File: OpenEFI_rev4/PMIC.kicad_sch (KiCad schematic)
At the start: 40 parts, among them U1 MCZ33810EK, U21 TC4424A, U24 TC4424A, U29 TC4424A, U30 TC4424A

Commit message: update sensors/connector pinout, added rtc vbatt backup
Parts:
- removed R129, R83: 10k, Resistor_SMD:R_0805_2012Metric, symbol Device:R
- added R58 (x2): 10k, Resistor_SMD:R_0805_2012Metric, symbol Device:R_Small
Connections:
- net GND: now also R58.1, R58.1
- net PMIC1_ENABLE: now also R58.2, R58.2
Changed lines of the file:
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@@
     (stroke (width 0) (type default))
   )
-  (wire (pts (xy 51.435 141.605) (xy 51.435 142.875))
+  (wire (pts (xy 48.26 143.51) (xy 48.26 144.78))
     (stroke (width 0) (type default))
   )
@@
     (stroke (width 0) (type solid))
   )
-  (wire (pts (xy 49.53 52.07) (xy 49.53 53.34))
+  (wire (pts (xy 49.53 54.61) (xy 49.53 55.88))
     (stroke (width 0) (type default))
   )
@@
     (effects (font (size 0.8 0.8)) (justify right bottom))
   )
-  (label "PMIC1_ENABLE" (at 51.435 141.605 180) (fields_autoplaced)
+  (label "PMIC1_ENABLE" (at 48.26 143.51 180) (fields_autoplaced)
     (effects (font (size 0.7874 0.7874)) (justify right bottom))
   )
-  (label "PMIC1_ENABLE" (at 49.53 52.07 180) (fields_autoplaced)
+  (label "PMIC1_ENABLE" (at 49.53 54.61 180) (fields_autoplaced)
     (effects (font (size 0.7874 0.7874)) (justify right bottom))
   )
@@
     )
   )
-  (symbol (lib_name "GND_1") (lib_id "power:GND") (at 51.435 150.495 0) (unit 1)
+  (symbol (lib_name "GND_1") (lib_id "power:GND") (at 48.26 149.86 0) (unit 1)
     (in_bom yes) (on_board yes) (dnp no) (fields_autoplaced)
-    (property "Reference" "#PWR02" (at 51.435 156.845 0)
+    (property "Reference" "#PWR02" (at 48.26 156.21 0)
       (effects (font (size 1.27 1.27)) hide)
     )
-    (property "Value" "GND" (at 51.435 154.94 0)
+    (property "Value" "GND" (at 48.26 154.305 0)
       (effects (font (size 1.27 1.27)))
     )
-    (property "Footprint" "" (at 51.435 150.495 0)
+    (property "Footprint" "" (at 48.26 149.86 0)
       (effects (font (size 1.27 1.27)) hide)
     )
-    (property "Datasheet" "" (at 51.435 150.495 0)
+    (property "Datasheet" "" (at 48.26 149.86 0)
       (effects (font (size 1.27 1.27)) hide)
     )
@@
     )
   )
+  (symbol (lib_id "Device:R_Small") (at 49.53 58.42 0) (mirror x) (unit 1)
+    (in_bom yes) (on_board yes) (dnp no)
+    (property "Reference" "R58" (at 51.435 58.42 90)
+      (effects (font (size 1.27 1.27)))
+    )
+    (property "Value" "10k" (at 47.625 58.42 90)
+      (effects (font (size 1.27 1.27)))
+    )
+    (property "Footprint" "Resistor_SMD:R_0805_2012Metric" (at 49.53 58.42 0)
+      (effects (font (size 1.27 1.27)) hide)
+    )
+    (property "Datasheet" "~" (at 49.53 58.42 0)
+      (effects (font (size 1.27 1.27)) hide)
+    )
+    (property "LCSC" "C17414" (at 49.53 58.42 90)
+      (effects (font (size 0.889 0.889)) hide)
+    )
+    (pin "1")
+    (pin "2")
+    (instances
+      (project "OpenEFI_rev4"
+        (path "/b282ce4b-c3d0-4c94-b06c-73b92bb672a9"
+          (reference "R58") (unit 1)
+        )
+        (path "/b282ce4b-c3d0-4c94-b06c-73b92bb672a9/00000000-0000-0000-0000-00005fa9324b"
+          (reference "R84") (unit 1)
+        )
+      )
+    )
+  )
   (symbol (lib_id "OpenEFI-STM32-rev3:MCZ33810EK") (at 78.105 51.435 0) (unit 1)
     (in_bom yes) (on_board yes) (dnp no)
@@
     )
   )
-  (symbol (lib_id "Device:R") (at 49.53 57.15 180) (unit 1)
-    (in_bom yes) (on_board yes) (dnp no)
-    (property "Reference" "R129" (at 47.752 58.3184 0)
-      (effects (font (size 1.27 1.27)) (justify left))
-    )
-    (property "Value" "10k" (at 47.752 56.007 0)
-      (effects (font (size 1.27 1.27)) (justify left))
-    )
-    (property "Footprint" "Resistor_SMD:R_0805_2012Metric" (at 51.308 57.15 90)
-      (effects (font (size 1.27 1.27)) hide)
-    )
-    (property "Datasheet" "~" (at 49.53 57.15 0)
-      (effects (font (size 1.27 1.27)) hide)
-    )
-    (property "Digikey Part Number" "311-10KARCT-ND" (at 49.53 57.15 0)
-      (effects (font (size 1.27 1.27)) hide)
-    )
-    (property "Manufacturer_Name" "Yageo" (at 49.53 57.15 0)
-      (effects (font (size 1.27 1.27)) hide)
-    )
-    (property "Manufacturer_Part_Number" "RC0805JR-0710KL" (at 49.53 57.15 0)
-      (effects (font (size 1.27 1.27)) hide)
-    )
-    (property "URL" "https://www.digikey.com/product-detail/en/yageo/RC0805JR-0710KL/311-10KARCT-ND/731188" (at 49.53 57.15 0)
-      (effects (font (size 1.27 1.27)) hide)
-    )
-    (pin "1")
-    (pin "2")
-    (instances
-      (project "OpenEFI_rev4"
-        (path "/b282ce4b-c3d0-4c94-b06c-73b92bb672a9/00000000-0000-0000-0000-00005fa9324b"
-          (reference "R129") (unit 1)
-        )
-      )
-      (project "DropBear"
-        (path "/ebe274a6-1c43-4fa2-9d2a-7756c5a7217c/00000000-0000-0000-0000-00005cb195fe"
-          (reference "R6") (unit 1)
-        )
-      )
-    )
-  )
   (symbol (lib_id "power:GND") (at 257.175 97.79 0) (unit 1)
     (in_bom yes) (on_board yes) (dnp no)
@@
     )
   )
-  (symbol (lib_id "Device:R") (at 51.435 146.685 180) (unit 1)
-    (in_bom yes) (on_board yes) (dnp no)
-    (property "Reference" "R83" (at 49.657 147.8534 0)
-      (effects (font (size 1.27 1.27)) (justify left))
-    )
-    (property "Value" "10k" (at 49.657 145.542 0)
-      (effects (font (size 1.27 1.27)) (justify left))
-    )
-    (property "Footprint" "Resistor_SMD:R_0805_2012Metric" (at 53.213 146.685 90)
-      (effects (font (size 1.27 1.27)) hide)
-    )
-    (property "Datasheet" "~" (at 51.435 146.685 0)
-      (effects (font (size 1.27 1.27)) hide)
-    )
-    (property "Digikey Part Number" "311-10KARCT-ND" (at 51.435 146.685 0)
-      (effects (font (size 1.27 1.27)) hide)
-    )
-    (property "Manufacturer_Name" "Yageo" (at 51.435 146.685 0)
-      (effects (font (size 1.27 1.27)) hide)
-    )
-    (property "Manufacturer_Part_Number" "RC0805JR-0710KL" (at 51.435 146.685 0)
-      (effects (font (size 1.27 1.27)) hide)
-    )
-    (property "URL" "https://www.digikey.com/product-detail/en/yageo/RC0805JR-0710KL/311-10KARCT-ND/731188" (at 51.435 146.685 0)
-      (effects (font (size 1.27 1.27)) hide)
-    )
-    (pin "1")
-    (pin "2")
-    (instances
-      (project "OpenEFI_rev4"
-        (path "/b282ce4b-c3d0-4c94-b06c-73b92bb672a9/00000000-0000-0000-0000-00005fa9324b"
-          (reference "R83") (unit 1)
-        )
-      )
-      (project "DropBear"
-        (path "/ebe274a6-1c43-4fa2-9d2a-7756c5a7217c/00000000-0000-0000-0000-00005cb195fe"
-          (reference "R6") (unit 1)
-        )
-      )
-    )
-  )
   (symbol (lib_id "Device:LED") (at 237.49 91.44 90) (unit 1)
     (in_bom yes) (on_board yes) (dnp no)
@@
         )
       )
+    )
+  )
+  (symbol (lib_id "Device:R_Small") (at 48.26 147.32 0) (mirror x) (unit 1)
+    (in_bom yes) (on_board yes) (dnp no)
+    (property "Reference" "R58" (at 50.165 147.32 90)
+      (effects (font (size 1.27 1.27)))
+    )
+    (property "Value" "10k" (at 46.355 147.32 90)
+      (effects (font (size 1.27 1.27)))
+    )
+    (property "Footprint" "Resistor_SMD:R_0805_2012Metric" (at 48.26 147.32 0)
+      (effects (font (size 1.27 1.27)) hide)
+    )
+    (property "Datasheet" "~" (at 48.26 147.32 0)
+      (effects (font (size 1.27 1.27)) hide)
+    )
+    (property "LCSC" "C17414" (at 48.26 147.32 90)
+      (effects (font (size 0.889 0.889)) hide)
+    )
+    (pin "1")
+    (pin "2")
+    (instances
+      (project "OpenEFI_rev4"
+        (path "/b282ce4b-c3d0-4c94-b06c-73b92bb672a9"
+          (reference "R58") (unit 1)
+        )
+        (path "/b282ce4b-c3d0-4c94-b06c-73b92bb672a9/00000000-0000-0000-0000-00005fa9324b"
+          (reference "R83") (unit 1)
+        )
+      )

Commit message: WIP Analog frontend
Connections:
- net INJ1: no longer D70.1 (K), U1.1 (OUT0)
- net INJ2: no longer D72.1 (K), U1.16 (OUT1)
- net INJ3: no longer D74.1 (K), U1.32 (OUT2)
- net INJ4: no longer D76.1 (K), U1.17 (OUT3)
- net PMIC1_ENABLE: no longer R58.2
- net PMIC2_ENABLE: now also R58.2
- new net INJ5: D70.1 (K), U1.1 (OUT0)
- new net INJ6: D72.1 (K), U1.16 (OUT1)
- new net INJ7: D74.1 (K), U1.32 (OUT2)
- new net INJ8: D76.1 (K), U1.17 (OUT3)
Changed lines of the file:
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@@
   (title_block
     (title "OpenEFI")
-    (date "2023-10-13")
+    (date "2023-10-14")
     (rev "4.0")
     (company "Churrosoft®")
@@
     (effects (font (size 2 2)) (justify left bottom))
   )
-  (label "OUT3" (at 100.965 143.51 180) (fields_autoplaced)
-    (effects (font (size 0.8 0.8)) (justify right bottom))
-  )
   (label "GD1" (at 102.235 115.57 180) (fields_autoplaced)
     (effects (font (size 0.8 0.8)) (justify right bottom))
@@
   )
   (label "OUT1" (at 100.965 57.15 180) (fields_autoplaced)
-    (effects (font (size 0.8 0.8)) (justify right bottom))
-  )
-  (label "OUT0" (at 100.965 135.89 180) (fields_autoplaced)
     (effects (font (size 0.8 0.8)) (justify right bottom))
   )
@@
     (effects (font (size 0.7874 0.7874)) (justify right bottom))
   )
-  (label "PMIC1_ENABLE" (at 49.53 54.61 180) (fields_autoplaced)
+  (label "PMIC2_ENABLE" (at 49.53 54.61 180) (fields_autoplaced)
     (effects (font (size 0.7874 0.7874)) (justify right bottom))
   )
-  (label "OUT1" (at 100.965 138.43 180) (fields_autoplaced)
-    (effects (font (size 0.8 0.8)) (justify right bottom))
-  )
   (label "FB2" (at 99.695 69.85 180) (fields_autoplaced)
     (effects (font (size 0.8 0.8)) (justify right bottom))
@@
     (effects (font (size 0.8 0.8)) (justify right bottom))
   )
-  (label "OUT2" (at 100.965 140.97 180) (fields_autoplaced)
-    (effects (font (size 0.8 0.8)) (justify right bottom))
-  )

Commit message: WIP CKP/CMP
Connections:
- net GD0: no longer U1.3 (GD0), U21.2 (IN_A)
- net GD1: no longer U1.14 (GD1), U21.4 (IN_B)
- net GD2: no longer U1.30 (GD2), U24.2 (IN_A)
- net GD3: no longer U1.19 (GD3), U24.4 (IN_B)
- net FB0: no longer names the net of U1.2 (FB0)
- net FB0: no longer U1.2 (FB0)
- net FB1: no longer names the net of U1.15 (FB1)
- net FB1: no longer U1.15 (FB1)
- net FB2: no longer names the net of U1.31 (FB2)
- net FB2: no longer U1.31 (FB2)
- net FB3: no longer names the net of U1.18 (FB3)
- net FB3: no longer U1.18 (FB3)
- new net: U1.30 (GD2), U24.2 (IN_A)
- new net: U1.19 (GD3), U24.4 (IN_B)
- new net: U1.14 (GD1), U21.4 (IN_B)
- new net: U1.3 (GD0), U21.2 (IN_A)
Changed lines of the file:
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@@
     (effects (font (size 2 2)) (justify left bottom))
-  )
-  (label "GD1" (at 102.235 115.57 180) (fields_autoplaced)
-    (effects (font (size 0.8 0.8)) (justify right bottom))
   )
   (label "OUT3" (at 100.965 62.23 180) (fields_autoplaced)
     (effects (font (size 0.8 0.8)) (justify right bottom))
   )
-  (label "FB1" (at 99.695 72.39 180) (fields_autoplaced)
-    (effects (font (size 0.8 0.8)) (justify right bottom))
-  )
   (label "OUT0" (at 100.965 54.61 180) (fields_autoplaced)
-    (effects (font (size 0.8 0.8)) (justify right bottom))
-  )
-  (label "FB3" (at 99.695 148.59 180) (fields_autoplaced)
-    (effects (font (size 0.8 0.8)) (justify right bottom))
-  )
-  (label "FB2" (at 99.695 151.13 180) (fields_autoplaced)
     (effects (font (size 0.8 0.8)) (justify right bottom))
   )
@@
     (effects (font (size 0.7874 0.7874)) (justify right bottom))
   )
-  (label "FB2" (at 99.695 69.85 180) (fields_autoplaced)
-    (effects (font (size 0.8 0.8)) (justify right bottom))
-  )
-  (label "FB3" (at 99.695 67.31 180) (fields_autoplaced)
-    (effects (font (size 0.8 0.8)) (justify right bottom))
-  )
-  (label "GD3" (at 102.235 120.65 180) (fields_autoplaced)
-    (effects (font (size 0.8 0.8)) (justify right bottom))
-  )
-  (label "GD2" (at 102.235 118.11 180) (fields_autoplaced)
-    (effects (font (size 0.8 0.8)) (justify right bottom))
-  )
-  (label "FB0" (at 99.695 156.21 180) (fields_autoplaced)
-    (effects (font (size 0.8 0.8)) (justify right bottom))
-  )
   (label "GD0" (at 102.235 31.75 180) (fields_autoplaced)
-    (effects (font (size 0.8 0.8)) (justify right bottom))
-  )
-  (label "FB0" (at 99.695 74.93 180) (fields_autoplaced)
-    (effects (font (size 0.8 0.8)) (justify right bottom))
-  )
-  (label "FB1" (at 99.695 153.67 180) (fields_autoplaced)
     (effects (font (size 0.8 0.8)) (justify right bottom))
   )
@@
     (effects (font (size 0.8 0.8)) (justify right bottom))
   )
-  (label "GD0" (at 102.235 113.03 180) (fields_autoplaced)
-    (effects (font (size 0.8 0.8)) (justify right bottom))
-  )

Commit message: Rev4 WIP LCSC assigments
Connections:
- net at D71.2 (A): now also RN2.3 (R3.1); no longer RN2.2 (R2.1)
- net at D69.2 (A): now also RN2.4 (R4.1); no longer RN2.1 (R1.1)
- net at D73.2 (A): now also RN2.2 (R2.1); no longer RN2.3 (R3.1)
- net at D75.2 (A): now also RN2.1 (R1.1); no longer RN2.4 (R4.1)
- net at RN1.1 (R1.1): now also D67.2 (A); no longer D43.2 (A)
- net at RN1.2 (R2.1): now also D65.2 (A); no longer D63.2 (A)
- net at RN1.3 (R3.1): now also D63.2 (A); no longer D65.2 (A)
- net at RN1.4 (R4.1): now also D43.2 (A); no longer D67.2 (A)
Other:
- moved on the sheet: D43, D47, D65, D66, D67, D68, RN1, RN2

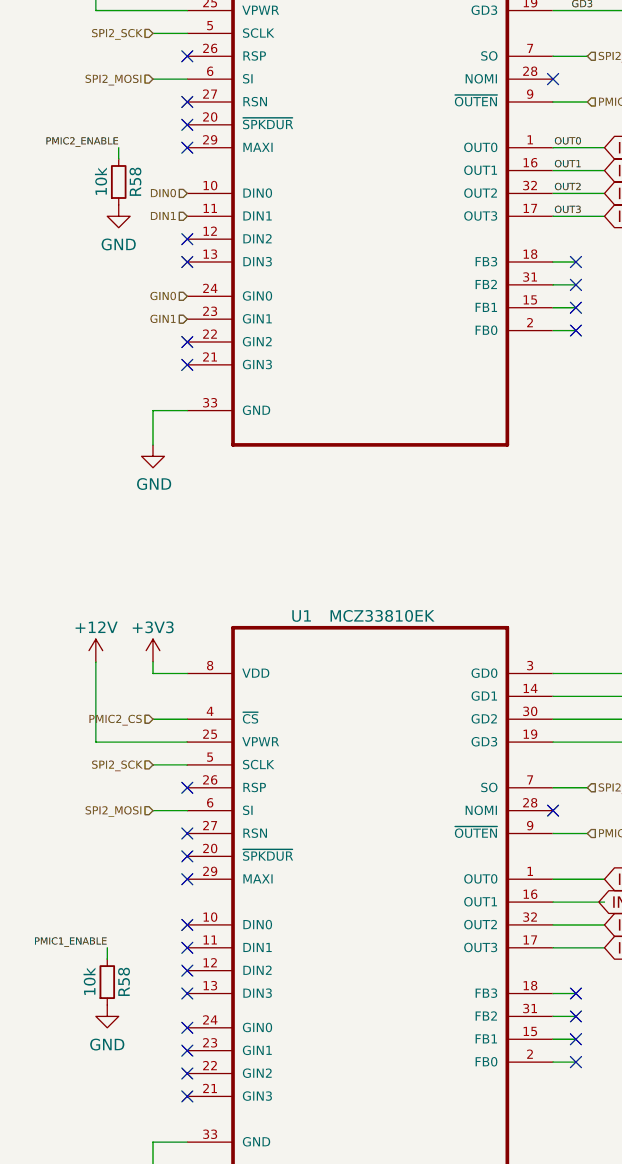
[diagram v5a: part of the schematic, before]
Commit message: update 32khz crystal
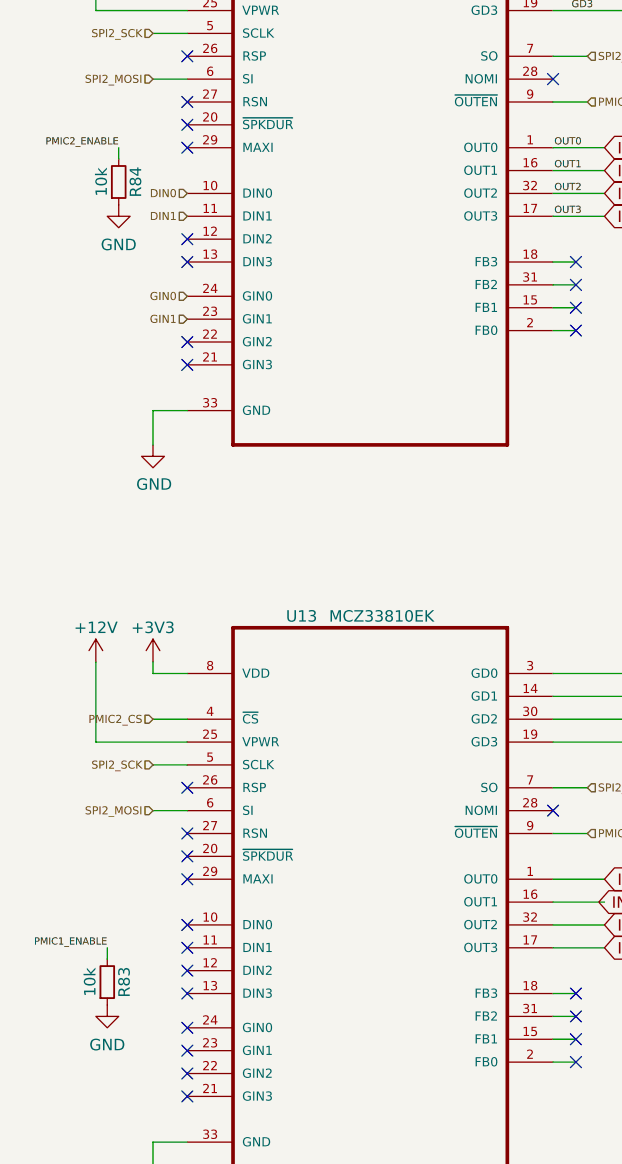
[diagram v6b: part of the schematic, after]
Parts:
- renumbered R58 to R83, R58 to R84, U1 to U13
